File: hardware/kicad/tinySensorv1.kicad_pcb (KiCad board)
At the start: 2 copper layers, 19 parts, among them J1 RADIO, J10 CR2032 socket, J11 AAA socket, J12 AA Socket, J13 Bornier, J2 DCDC converter, J3 BMP/BME breakout, J5 OneWire sensor, J6 ISP, J7 Analog sensor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

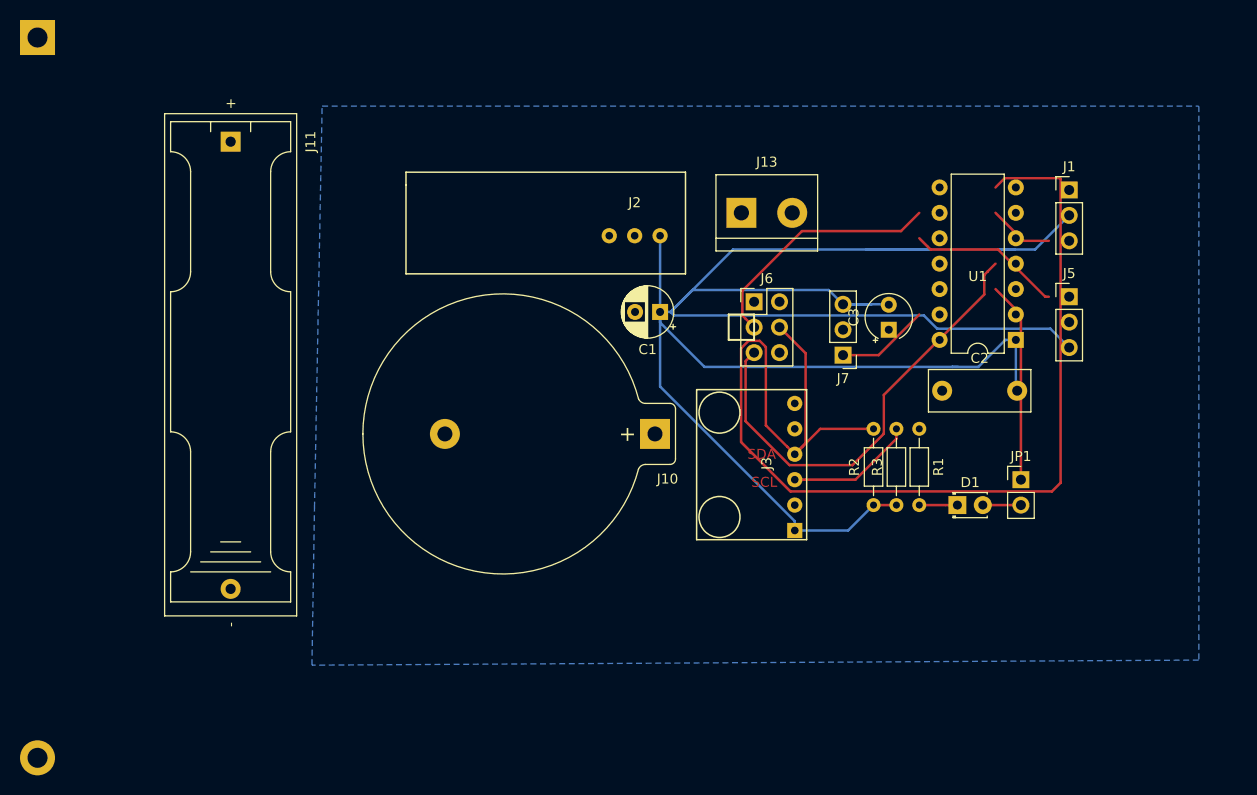
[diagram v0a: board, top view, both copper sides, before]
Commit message: Updated card layout
* Use new ICSP footprint
* Better capacitor footprint
* board limits
* removed all tracks, to be refined
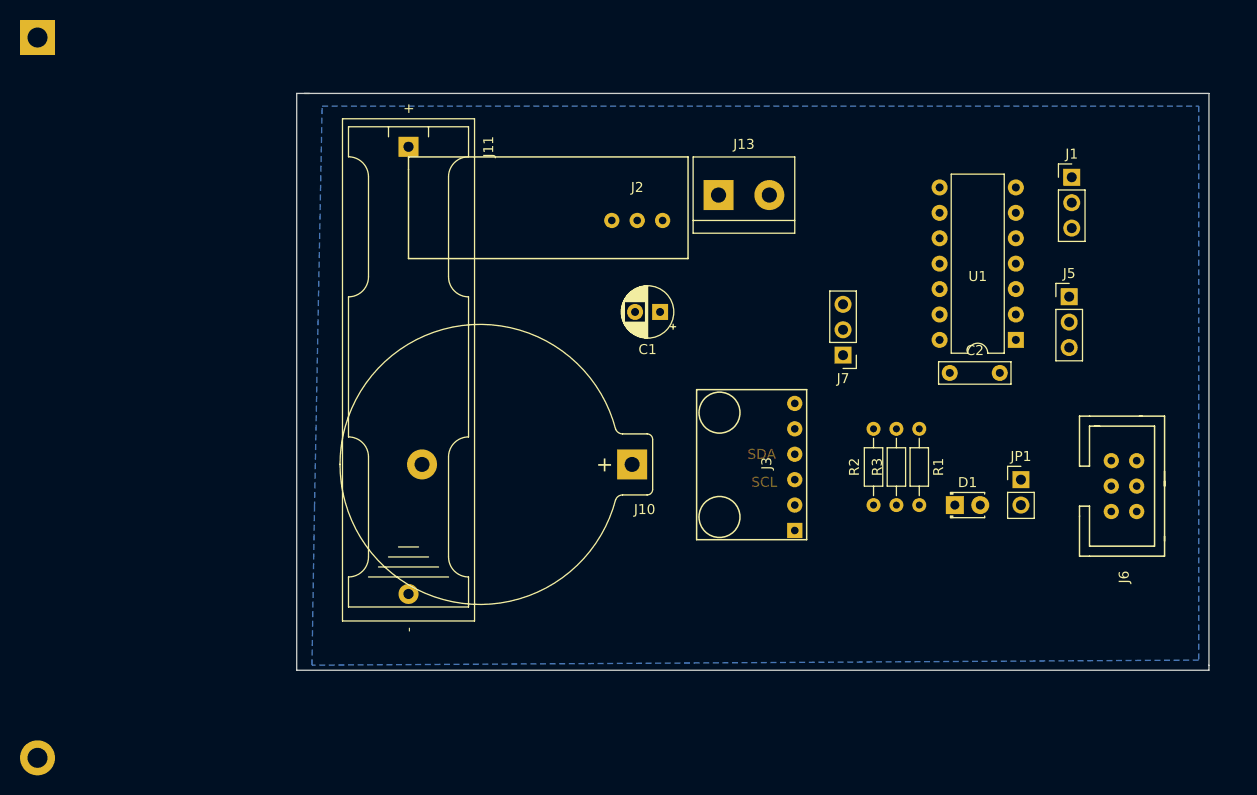
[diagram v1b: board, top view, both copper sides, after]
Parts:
- removed C3: 0.1n, Capacitor_THT:CP_Radial_Tantal_D4.5mm_P2.50mm
- C2: footprint Capacitor_THT:C_Rect_L10.0mm_W4.0mm_P7.50mm_FKS3_FKP3 -> Capacitor_THT:C_Rect_L7.0mm_W2.0mm_P5.00mm
- J2: footprint Chinese breakouts:DC-DC 0.9v-3.3v to 3.3v -> TinySensor lib:DC-DC_0.9v-3.3v_to_3.3v
- J3: footprint Chinese breakouts:BMx280 breakout -> TinySensor lib:BMx280_breakout
- J6: footprint Connector_PinHeader_2.54mm:PinHeader_2x03_P2.54mm_Vertical -> TinySensor lib:ICSP_SOCKET_MINI_2x3
- moved J6 35.4 mm to (192.3, 78.7), turned to 270 degrees
- moved J11 17.8 mm to (124.2, 51.8)
- moved J10 3.81 mm to (146.6, 83.6)
- moved J13 2.90 mm to (155.2, 56.6)
- moved C2 1.93 mm to (178.3, 74.4)
- moved J2 1.55 mm to (147.1, 55.4)
- moved J1 1.30 mm to (190.5, 54.9)
- moved D1 0.25 mm to (178.8, 87.6)
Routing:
- net +3V3: track 218.7 -> 0.00 mm
- net /SDA: track 119.1 -> 0.00 mm
- net /RESET: track 45.8 -> 0.00 mm
- net /SCL: track 37.9 -> 0.00 mm
- net /LED_OUT: track 20.1 -> 0.00 mm
- net /OneWire: track 15.4 -> 0.00 mm
- net /Analog_sensor: track 9.30 -> 0.00 mm
- net Net-(U1-Pad5): track 6.49 -> 0.00 mm
- net Net-(D1-Pad1): track 3.81 -> 0.00 mm
- net Net-(D1-Pad2): track 3.81 -> 0.00 mm
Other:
- board outline added: 91.2 x 57.7 mm

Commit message: Finish a first version of PCB layout
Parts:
- added C3: 1u, Capacitor_THT:CP_Radial_D4.0mm_P1.50mm, F.Cu at (162.3, 66.8)
- added JP2: Direct alim, Connector_PinHeader_2.54mm:PinHeader_1x02_P2.54mm_Vertical, F.Cu at (144.0, 54.0)
- added R4: 75R, Resistor_THT:R_Axial_DIN0204_L3.6mm_D1.6mm_P7.62mm_Horizontal, F.Cu at (167.1, 72.9)
- added R6: 4k7, Resistor_THT:R_Axial_DIN0204_L3.6mm_D1.6mm_P7.62mm_Horizontal, F.Cu at (160.8, 59.9)
- moved J12 124.3 mm to (199.0, 95.0), turned to 180 degrees
- moved J1 26.8 mm to (198.4, 80.5), turned to 180 degrees
- moved J6 26.5 mm to (194.8, 52.3)
- moved J10 25.1 mm to (130.8, 64.0), turned to 270 degrees
- moved R3 24.6 mm to (193.5, 74.2), turned to 270 degrees
- moved R2 24.4 mm to (191.0, 74.2), turned to 270 degrees
- moved C1 22.8 mm to (165.9, 52.6)
- moved J3 22.4 mm to (181.4, 86.1), turned to 180 degrees
- moved R1 19.3 mm to (156.2, 83.0), turned to 0 degrees
- moved D1 18.5 mm to (163.0, 78.0)
- moved J5 18.4 mm to (173.2, 59.7), turned to 180 degrees
- moved J13 16.5 mm to (139.0, 53.6), turned to 180 degrees
- moved JP1 14.3 mm to (173.0, 78.0), turned to 270 degrees
- moved J7 5.59 mm to (173.2, 72.9)
- moved U1 5.00 mm to (189.5, 69.1)
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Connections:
- U1 pad 2: Net-(U1-Pad2) -> /TX_RADIO
- U1 pad 6: /TX_RADIO -> /PWM_OUT
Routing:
- net GND: track 0.00 -> 228.4 mm
- net +BATT: track 0.00 -> 224.3 mm
- net +3V3: track 0.00 -> 146.1 mm
- net /SCL: track 0.00 -> 68.0 mm
- net /SDA: track 0.00 -> 63.6 mm
- net /LED_OUT: track 0.00 -> 23.3 mm
- net /Analog_sensor: track 0.00 -> 17.4 mm
- net /MISO: track 0.00 -> 16.3 mm
- net /OneWire: track 0.00 -> 13.9 mm
- net /TX_RADIO: track 0.00 -> 12.6 mm
- net Net-(C3-Pad1): track 0.00 -> 7.75 mm
- net /RESET: track 0.00 -> 7.67 mm
- net Net-(D1-Pad1): track 0.00 -> 5.34 mm
- net Net-(D1-Pad2): track 0.00 -> 4.92 mm
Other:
- board size 91.2 x 57.7 mm -> 92 x 60 mm
- board text removed: "SCL"
- board text removed: "SDA"

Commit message: Initial hardware version (first batch)
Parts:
- added C4: 1n, Capacitor_THT:CP_Radial_Tantal_D4.5mm_P2.50mm, F.Cu at (198.6, 76.2)
- added MH1: MountingHole, MountingHole:MountingHole_2.5mm, F.Cu at (203.0, 52.0)
- added MH2: MountingHole, MountingHole:MountingHole_2.5mm, F.Cu at (160.0, 84.0)
- added MH3: MountingHole, MountingHole:MountingHole_2.5mm, F.Cu at (203.0, 84.0)
- added MH4: MountingHole, MountingHole:MountingHole_2.5mm, F.Cu at (121.0, 51.8)
- added MH5: MountingHole, MountingHole:MountingHole_2.5mm, F.Cu at (160.0, 51.8)
- added MH6: MountingHole, MountingHole:MountingHole_2.5mm, F.Cu at (121.0, 84.0)
- added MH7: MountingHole, MountingHole:MountingHole_2.5mm, F.Cu at (160.0, 96.8)
- JP2: value Direct alim -> DIRECT Vcc; footprint Connector_PinHeader_2.54mm:PinHeader_1x02_P2.54mm_Vertical -> Jumper:SolderJumper-2_P1.3mm_Open_TrianglePad1.0x1.5mm
- moved J11 87.7 mm to (200.0, 97.0), turned to 180 degrees
- moved R3 34.3 mm to (166.9, 52.6), turned to 0 degrees
- moved J13 22.3 mm to (150.0, 73.0), turned to 270 degrees
- moved R2 20.4 mm to (202.2, 57.1)
- moved J10 10.4 mm to (136.0, 55.0)
- moved R1 8.69 mm to (164.8, 82.0)
- moved J3 7.28 mm to (184.9, 79.8)
- moved J1 5.93 mm to (194.3, 76.2)
- moved C1 4.51 mm to (165.0, 57.0)
- moved C2 3.78 mm to (180.3, 71.6)
- moved D1 3.75 mm to (159.5, 76.7)
- moved J12 3.61 mm to (196.0, 97.0)
- moved J5 3.18 mm to (170.4, 61.2)
- moved J6 3.18 mm to (192.0, 53.8)
- moved JP1 3.18 mm to (170.2, 79.5)
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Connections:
- D1 pad 1: Net-(D1-Pad1) -> GND
- JP1 pad 2: Net-(D1-Pad2) -> Net-(JP1-Pad2)
- JP2 pad 1: +3V3 -> +BATT
- JP2 pad 2: +BATT -> +3V3
- R1 pad 1: GND -> Net-(D1-Pad2)
- R1 pad 2: Net-(D1-Pad1) -> Net-(JP1-Pad2)
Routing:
- net GND: track 228.4 -> 326.4 mm
- net +BATT: track 224.3 -> 194.2 mm
- net +3V3: track 146.1 -> 164.9 mm
- net Net-(JP1-Pad2): track 0.00 -> 5.84 mm
- net /SCL: track 68.0 -> 62.3 mm
- net Net-(D1-Pad1): track 5.34 -> 0.00 mm
- net Net-(C3-Pad1): track 7.75 -> 3.30 mm
- net /LED_OUT: track 23.3 -> 27.3 mm
- net /TX_RADIO: track 12.6 -> 9.83 mm
- net /OneWire: track 13.9 -> 16.2 mm
- net Net-(D1-Pad2): track 4.92 -> 6.55 mm
- net /Analog_sensor: track 17.4 -> 16.4 mm
- net /RESET: track 7.67 -> 8.62 mm
- net /MISO: track 16.3 -> 17.3 mm
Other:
- board size 92 x 60 mm -> 94 x 60 mm

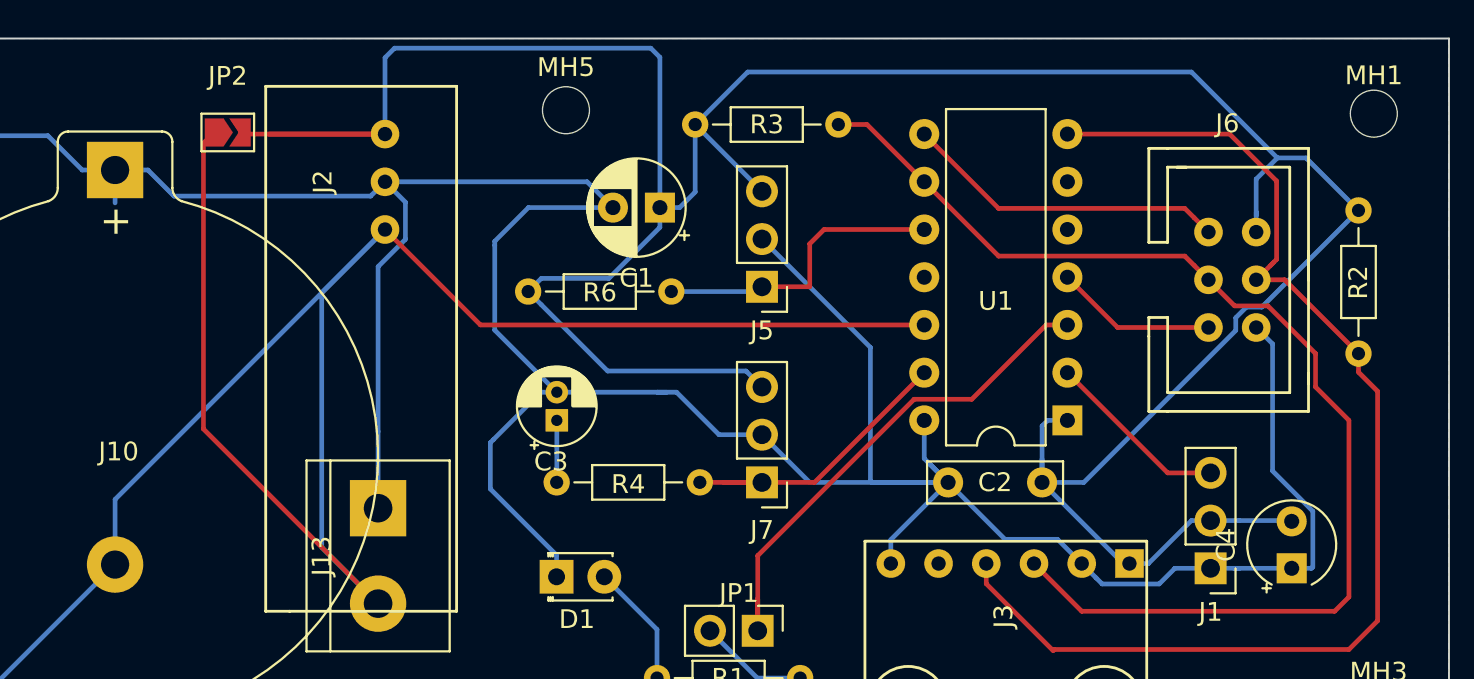
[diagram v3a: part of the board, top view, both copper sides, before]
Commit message: Avoid acid trap in traces (PCB)
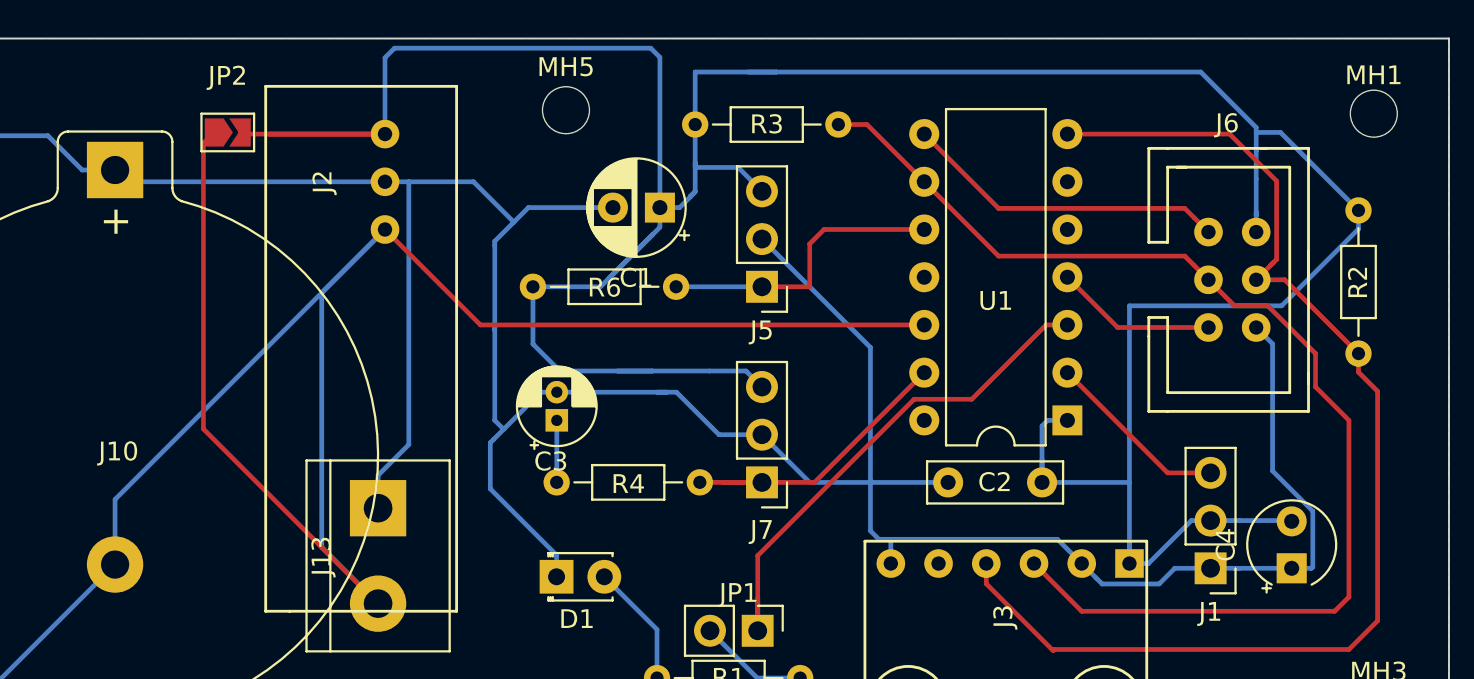
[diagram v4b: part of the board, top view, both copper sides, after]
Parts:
- moved R6 0.36 mm to (158.2, 61.2)
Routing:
- net +3V3: track 164.9 -> 179.8 mm
- net GND: track 326.4 -> 311.9 mm
